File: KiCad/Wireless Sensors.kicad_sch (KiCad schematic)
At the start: 1 part, among them U1 STM32L151C8T6

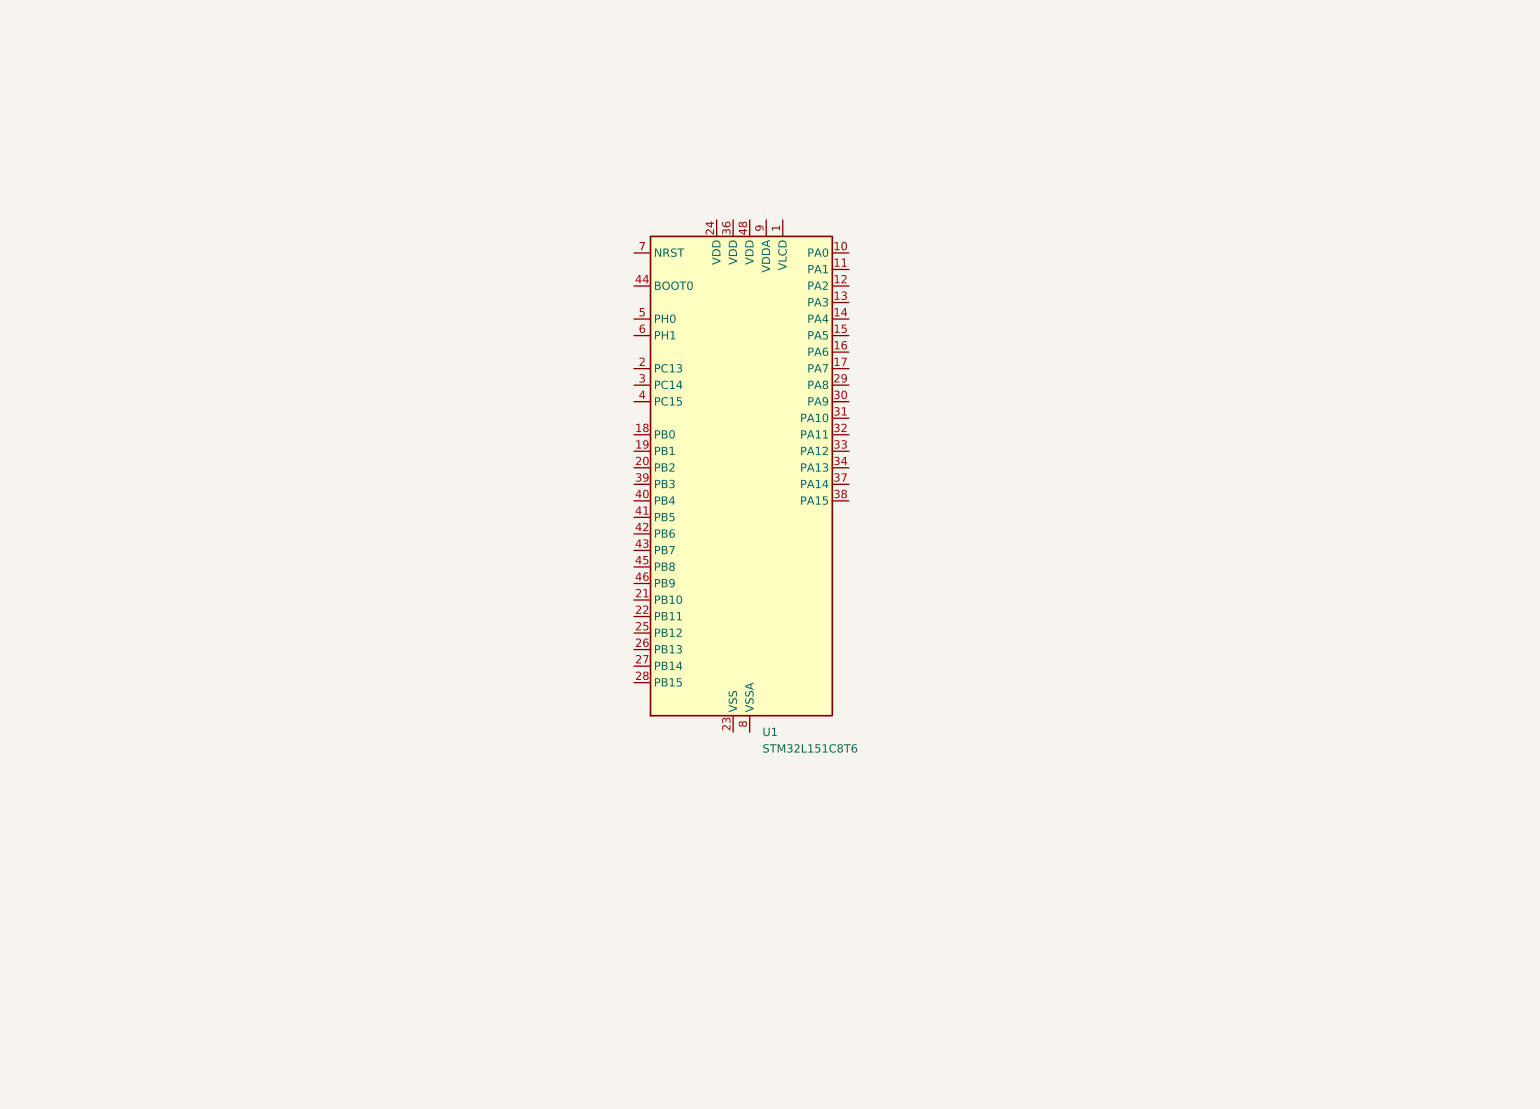
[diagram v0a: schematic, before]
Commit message: Updated schematic
First rev of complete CPU board schematic
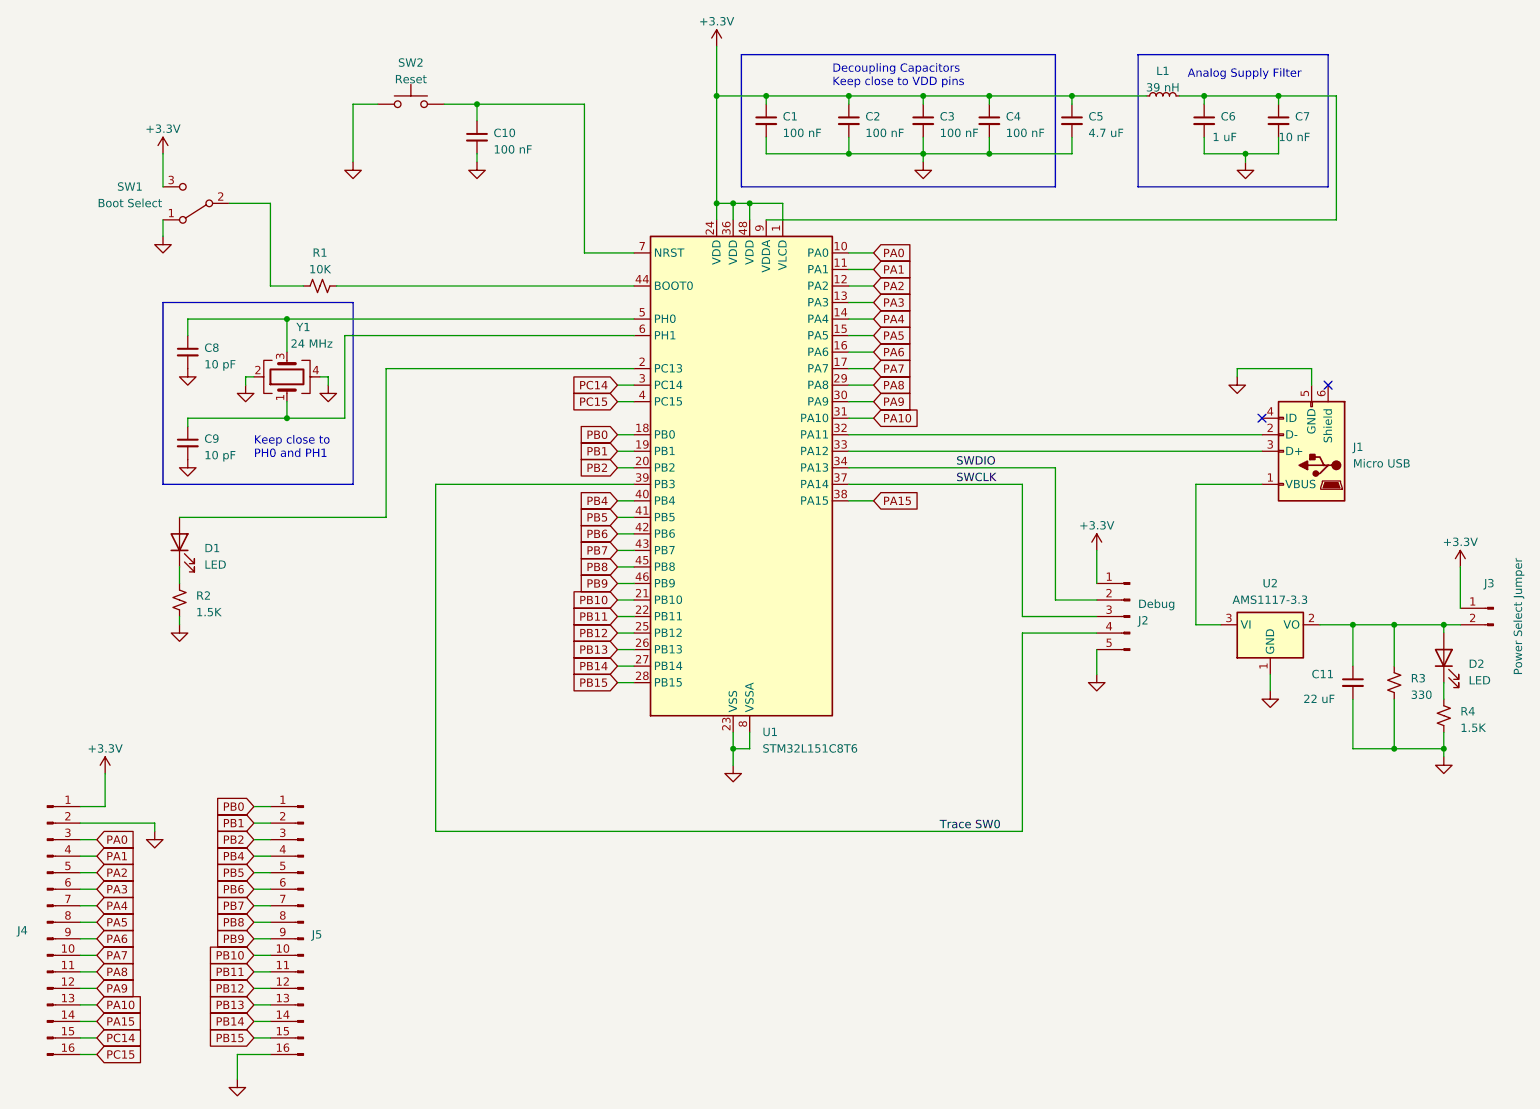
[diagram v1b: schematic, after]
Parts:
- added C1, C10, C2, C3, C4: 100 nF, symbol Device:C_Small
- added C11: 22 uF, symbol Device:C_Small
- added C5: 4.7 uF, symbol Device:C_Small
- added C6: 1 uF, symbol Device:C_Small
- added C7: 10 nF, symbol Device:C_Small
- added C8, C9: 10 pF, symbol Device:C_Small
- added D1, D2: LED, symbol Device:LED
- added J1: Micro USB, symbol Connector:USB_B_Micro
- added J2: Debug, symbol Connector:Conn_01x05_Pin
- added J3: Power Select Jumper, symbol Connector:Conn_01x02_Pin
- added J4, J5: Conn_01x16_Pin, symbol Connector:Conn_01x16_Pin
- added L1: 39 nH, symbol Device:L_Small
- added R1: 10K, symbol Device:R_Small_US
- added R2, R4: 1.5K, symbol Device:R_Small_US
- added R3: 330, symbol Device:R_Small_US
- added SW1: Boot Select, symbol Switch:SW_SPDT
- added SW2: Reset, symbol Switch:SW_Push
- added U2: AMS1117-3.3, Package_TO_SOT_SMD:SOT-223-3_TabPin2, symbol Regulator_Linear:AMS1117-3.3
- added Y1: 24 MHz, symbol Device:Crystal_GND24
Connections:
- net +3.3V: now reaches U1.1 (VLCD)
- net +3.3V: now also U1.24 (VDD), U1.36 (VDD), U1.48 (VDD), C1.1, C2.1, C3.1, C4.1, C5.1, J2.1 (Pin_1), J3.1 (Pin_1), J4.1 (Pin_1), L1.1, SW1.3 (C)
- net PA0: now reaches U1.10 (PA0)
- net PA0: now also J4.3 (Pin_3)
- net PA1: now reaches U1.11 (PA1)
- net PA1: now also J4.4 (Pin_4)
- net PA2: now reaches U1.12 (PA2)
- net PA2: now also J4.5 (Pin_5)
- net PA3: now reaches U1.13 (PA3)
- net PA3: now also J4.6 (Pin_6)
- net PA4: now reaches U1.14 (PA4)
- net PA4: now also J4.7 (Pin_7)
- net PA5: now reaches U1.15 (PA5)
- net PA5: now also J4.8 (Pin_8)
- net PA6: now reaches U1.16 (PA6)
- net PA6: now also J4.9 (Pin_9)
- net PA7: now reaches U1.17 (PA7)
- net PA7: now also J4.10 (Pin_10)
- net PB0: now reaches U1.18 (PB0)
- net PB0: now also J5.1 (Pin_1)
- net PB1: now reaches U1.19 (PB1)
- net PB1: now also J5.2 (Pin_2)
- net at U1.2 (PC13): now also D1.2 (A)
- net PB2: now reaches U1.20 (PB2)
- net PB2: now also J5.3 (Pin_3)
- net PB10: now reaches U1.21 (PB10)
- net PB10: now also J5.10 (Pin_10)
- net PB11: now reaches U1.22 (PB11)
- net PB11: now also J5.11 (Pin_11)
- net GND: now reaches U1.23 (VSS), U1.35 (VSS), U1.47 (VSS)
- net GND: now also U1.8 (VSSA), C1.2, C10.2, C11.2, C2.2, C3.2, C4.2, C5.2, C6.2, C7.2, C8.2, C9.2, J1.5 (GND), J2.5 (Pin_5), J4.2 (Pin_2), J5.16 (Pin_16), R2.2, R3.2, R4.2, SW1.1 (A), SW2.1, U2.1 (GND), Y1.2, Y1.4
- net PB12: now reaches U1.25 (PB12)
- net PB12: now also J5.12 (Pin_12)
- net PB13: now reaches U1.26 (PB13)
- net PB13: now also J5.13 (Pin_13)
- net PB14: now reaches U1.27 (PB14)
- net PB14: now also J5.14 (Pin_14)
- net PB15: now reaches U1.28 (PB15)
- net PB15: now also J5.15 (Pin_15)
- net PA8: now reaches U1.29 (PA8)
- net PA8: now also J4.11 (Pin_11)
- net PC14: now reaches U1.3 (PC14)
- net PC14: now also J4.15 (Pin_15)
- net PA9: now reaches U1.30 (PA9)
- net PA9: now also J4.12 (Pin_12)
- net PA10: now reaches U1.31 (PA10)
- net PA10: now also J4.13 (Pin_13)
- net at U1.32 (PA11): now also J1.2 (D-)
- net at U1.33 (PA12): now also J1.3 (D+)
- net SWDIO: now reaches U1.34 (PA13)
- net SWDIO: now also J2.2 (Pin_2)
- net SWCLK: now reaches U1.37 (PA14)
- net SWCLK: now also J2.3 (Pin_3)
- net PA15: now reaches U1.38 (PA15)
- net PA15: now also J4.14 (Pin_14)
- net Trace SW0: now reaches U1.39 (PB3)
- net Trace SW0: now also J2.4 (Pin_4)
- net PC15: now reaches U1.4 (PC15)
- net PC15: now also J4.16 (Pin_16)
- net PB4: now reaches U1.40 (PB4)
- net PB4: now also J5.4 (Pin_4)
- net PB5: now reaches U1.41 (PB5)
- net PB5: now also J5.5 (Pin_5)
- net PB6: now reaches U1.42 (PB6)
- net PB6: now also J5.6 (Pin_6)
- net PB7: now reaches U1.43 (PB7)
- net PB7: now also J5.7 (Pin_7)
- net at U1.44 (BOOT0): now also R1.2
- net PB8: now reaches U1.45 (PB8)
- net PB8: now also J5.8 (Pin_8)
- net PB9: now reaches U1.46 (PB9)
- net PB9: now also J5.9 (Pin_9)
- net at U1.5 (PH0): now also C8.1, Y1.3
- net at U1.6 (PH1): now also C9.1, Y1.1
- net at U1.7 (NRST): now also C10.1, SW2.2
- net at U1.9 (VDDA): now also C6.1, C7.1, L1.2
- new net: C11.1, D2.2 (A), J3.2 (Pin_2), R3.1, U2.2 (VO)
- new net: R1.1, SW1.2 (B)
- new net: D2.1 (K), R4.1
- new net: D1.1 (K), R2.1
- new net: J1.1 (VBUS), U2.3 (VI)
- no-connect marks 0 -> 2
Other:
- note added: "Analog Supply Filter"
- note added: "Decoupling Capacitors Keep close to VDD pins"
- note added: "Keep close to PH0 and PH1"

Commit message: Complete CPU board
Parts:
- removed SW1: Boot Select, symbol Switch:SW_SPDT
- added C12: 1 uF, symbol Device:C_Small
- added J6: Boot Select, symbol Connector:Conn_01x03_Pin
- L1: value 39 nH -> 68 nH
- Y1: value 24 MHz -> 16 MHz
- renumbered SW2 to SW1
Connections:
- net +3.3V: now also J6.1 (Pin_1)
- net GND: now also C12.2, J6.3 (Pin_3)
- net at R1.1: now also J6.2 (Pin_2)
- net at J1.1 (VBUS), U2.3 (VI): now also C12.1
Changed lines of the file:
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@@
   (junction (at 189.23 30.48) (diameter 0) (color 0 0 0 0)
+  )
+  (junction (at 208.28 111.76) (diameter 0) (color 0 0 0 0)
   )
   (junction (at 139.7 46.99) (diameter 0) (color 0 0 0 0)
@@
     (stroke (width 0) (type default))
   )
-  (wire (pts (xy 59.69 46.99) (xy 66.04 46.99))
+  (wire (pts (xy 57.15 46.99) (xy 66.04 46.99))
     (stroke (width 0) (type default))
   )
@@
     (stroke (width 0) (type default))
   )
-  (wire (pts (xy 49.53 49.53) (xy 49.53 52.07))
+  (wire (pts (xy 57.15 49.53) (xy 57.15 52.07))
     (stroke (width 0) (type default))
   )
@@
     (stroke (width 0) (type default))
   )
-  (wire (pts (xy 49.53 39.37) (xy 49.53 44.45))
+  (wire (pts (xy 57.15 39.37) (xy 57.15 44.45))
     (stroke (width 0) (type default))
   )
@@
     (stroke (width 0) (type default))
   )
+  (wire (pts (xy 208.28 123.19) (xy 208.28 130.81))
+    (stroke (width 0) (type default))
+  )
   (wire (pts (xy 154.94 77.47) (xy 158.75 77.47))
     (stroke (width 0) (type default))
@@
   )
   (wire (pts (xy 238.76 111.76) (xy 238.76 118.11))
+    (stroke (width 0) (type default))
+  )
+  (wire (pts (xy 208.28 111.76) (xy 208.28 118.11))
     (stroke (width 0) (type default))
   )
@@
   (symbol (lib_id "Switch:SW_Push") (at 87.63 31.75 0) (unit 1)
     (in_bom yes) (on_board yes) (dnp no) (fields_autoplaced)
-    (property "Reference" "SW2" (at 87.63 25.4 0)
+    (property "Reference" "SW1" (at 87.63 25.4 0)
       (effects (font (size 1.27 1.27)))
     )
@@
       (project "Wireless Sensors"
         (path "/e76383f3-8840-49f1-acbc-452e4fcfbf34"
-          (reference "SW2") (unit 1)
+          (reference "SW1") (unit 1)
         )
       )
@@
     )
   )
-  (symbol (lib_id "power:+3.3V") (at 49.53 39.37 0) (unit 1)
-    (in_bom yes) (on_board yes) (dnp no) (fields_autoplaced)
-    (property "Reference" "#PWR05" (at 49.53 43.18 0)
-      (effects (font (size 1.27 1.27)) hide)
-    )
-    (property "Value" "+3.3V" (at 49.53 35.56 0)
+  (symbol (lib_id "power:+3.3V") (at 57.15 39.37 0) (unit 1)
+    (in_bom yes) (on_board yes) (dnp no) (fields_autoplaced)
+    (property "Reference" "#PWR05" (at 57.15 43.18 0)
+      (effects (font (size 1.27 1.27)) hide)
+    )
+    (property "Value" "+3.3V" (at 57.15 35.56 0)
       (effects (font (size 1.27 1.27)))
     )
-    (property "Footprint" "" (at 49.53 39.37 0)
-      (effects (font (size 1.27 1.27)) hide)
-    )
-    (property "Datasheet" "" (at 49.53 39.37 0)
+    (property "Footprint" "" (at 57.15 39.37 0)
+      (effects (font (size 1.27 1.27)) hide)
+    )
+    (property "Datasheet" "" (at 57.15 39.37 0)
       (effects (font (size 1.27 1.27)) hide)
     )
@@
     )
   )
+  (symbol (lib_id "power:GND") (at 208.28 130.81 0) (unit 1)
+    (in_bom yes) (on_board yes) (dnp no) (fields_autoplaced)
+    (property "Reference" "#PWR023" (at 208.28 137.16 0)
+      (effects (font (size 1.27 1.27)) hide)
+    )
+    (property "Value" "GND" (at 208.28 135.89 0)
+      (effects (font (size 1.27 1.27)) hide)
+    )
+    (property "Footprint" "" (at 208.28 130.81 0)
+      (effects (font (size 1.27 1.27)) hide)
+    )
+    (property "Datasheet" "" (at 208.28 130.81 0)
+      (effects (font (size 1.27 1.27)) hide)
+    )
+    (pin "1")
+    (instances
+      (project "Wireless Sensors"
+        (path "/e76383f3-8840-49f1-acbc-452e4fcfbf34"
+          (reference "#PWR023") (unit 1)
+        )
+      )
+    )
+  )
   (symbol (lib_id "power:GND") (at 97.79 40.64 0) (unit 1)
     (in_bom yes) (on_board yes) (dnp no) (fields_autoplaced)
@@
         (path "/e76383f3-8840-49f1-acbc-452e4fcfbf34"
           (reference "#PWR012") (unit 1)
-        )
-      )
-    )
-  )
-  (symbol (lib_id "Switch:SW_SPDT") (at 54.61 46.99 180) (unit 1)
-    (in_bom yes) (on_board yes) (dnp no)
-    (property "Reference" "SW1" (at 44.45 44.45 0)
-      (effects (font (size 1.27 1.27)))
-    )
-    (property "Value" "Boot Select" (at 44.45 46.99 0)
-      (effects (font (size 1.27 1.27)))
-    )
-    (property "Footprint" "" (at 54.61 46.99 0)
-      (effects (font (size 1.27 1.27)) hide)
-    )
-    (property "Datasheet" "~" (at 54.61 46.99 0)
-      (effects (font (size 1.27 1.27)) hide)
-    )
-    (pin "1")
-    (pin "2")
-    (pin "3")
-    (instances
-      (project "Wireless Sensors"
-        (path "/e76383f3-8840-49f1-acbc-452e4fcfbf34"
-          (reference "SW1") (unit 1)
         )
       )
@@
       (effects (font (size 1.27 1.27)))
     )
-    (property "Value" "24 MHz" (at 72.39 68.58 90)
+    (property "Value" "16 MHz" (at 72.39 68.58 90)
       (effects (font (size 1.27 1.27)))
     )
@@
     )
   )
-  (symbol (lib_id "power:GND") (at 49.53 52.07 0) (unit 1)
-    (in_bom yes) (on_board yes) (dnp no) (fields_autoplaced)
-    (property "Reference" "#PWR04" (at 49.53 58.42 0)
-      (effects (font (size 1.27 1.27)) hide)
-    )
-    (property "Value" "GND" (at 49.53 57.15 0)
-      (effects (font (size 1.27 1.27)) hide)
-    )
-    (property "Footprint" "" (at 49.53 52.07 0)
-      (effects (font (size 1.27 1.27)) hide)
-    )
-    (property "Datasheet" "" (at 49.53 52.07 0)
+  (symbol (lib_id "power:GND") (at 57.15 52.07 0) (unit 1)
+    (in_bom yes) (on_board yes) (dnp no) (fields_autoplaced)
+    (property "Reference" "#PWR04" (at 57.15 58.42 0)
+      (effects (font (size 1.27 1.27)) hide)
+    )
+    (property "Value" "GND" (at 57.15 57.15 0)
+      (effects (font (size 1.27 1.27)) hide)
+    )
+    (property "Footprint" "" (at 57.15 52.07 0)
+      (effects (font (size 1.27 1.27)) hide)
+    )
+    (property "Datasheet" "" (at 57.15 52.07 0)
       (effects (font (size 1.27 1.27)) hide)
     )
@@
         (path "/e76383f3-8840-49f1-acbc-452e4fcfbf34"
           (reference "#PWR04") (unit 1)
+        )
+      )
+    )
+  )
+  (symbol (lib_id "Connector:Conn_01x03_Pin") (at 52.07 46.99 0) (unit 1)
+    (in_bom yes) (on_board yes) (dnp no)
+    (property "Reference" "J6" (at 44.45 45.72 0)
+      (effects (font (size 1.27 1.27)))
+    )
+    (property "Value" "Boot Select" (at 44.45 48.26 0)
+      (effects (font (size 1.27 1.27)))
+    )
+    (property "Footprint" "" (at 52.07 46.99 0)
+      (effects (font (size 1.27 1.27)) hide)
+    )
+    (property "Datasheet" "~" (at 52.07 46.99 0)
+      (effects (font (size 1.27 1.27)) hide)
+    )
+    (pin "1")
+    (pin "2")
+    (pin "3")
+    (instances
+      (project "Wireless Sensors"
+        (path "/e76383f3-8840-49f1-acbc-452e4fcfbf34"
+          (reference "J6") (unit 1)
         )
       )
@@
     )
   )
+  (symbol (lib_id "Device:C_Small") (at 208.28 120.65 0) (unit 1)
+    (in_bom yes) (on_board yes) (dnp no)
+    (property "Reference" "C12" (at 210.82 120.0213 0)
+      (effects (font (size 1.27 1.27)) (justify left))
+    )
+    (property "Value" "1 uF" (at 209.55 123.19 0)
+      (effects (font (size 1.27 1.27)) (justify left))
+    )
+    (property "Footprint" "" (at 208.28 120.65 0)
+      (effects (font (size 1.27 1.27)) hide)
+    )
+    (property "Datasheet" "~" (at 208.28 120.65 0)
+      (effects (font (size 1.27 1.27)) hide)
+    )
+    (pin "1")
+    (pin "2")
+    (instances
+      (project "Wireless Sensors"
+        (path "/e76383f3-8840-49f1-acbc-452e4fcfbf34"
+          (reference "C12") (unit 1)
+        )
+      )
+    )
+  )
   (symbol (lib_id "Device:L_Small") (at 203.2 30.48 90) (unit 1)
     (in_bom yes) (on_board yes) (dnp no) (fields_autoplaced)
@@
       (effects (font (size 1.27 1.27)))
     )
-    (property "Value" "39 nH" (at 203.2 29.21 90)
+    (property "Value" "68 nH" (at 203.2 29.21 90)
       (effects (font (size 1.27 1.27)))
     )
